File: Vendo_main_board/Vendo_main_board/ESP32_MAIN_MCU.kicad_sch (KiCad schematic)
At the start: 9 parts, among them SW1 SW_Push, SW2 SW_Push, U6 ESP32-WROOM-32

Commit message: -
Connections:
- no-connect marks 8 -> 10
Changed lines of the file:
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@@
+	)
+	(no_connect
+		(at 152.1704 95.8039)
+	)
+	(no_connect
+		(at 152.1704 78.0239)
 	)
 	(no_connect

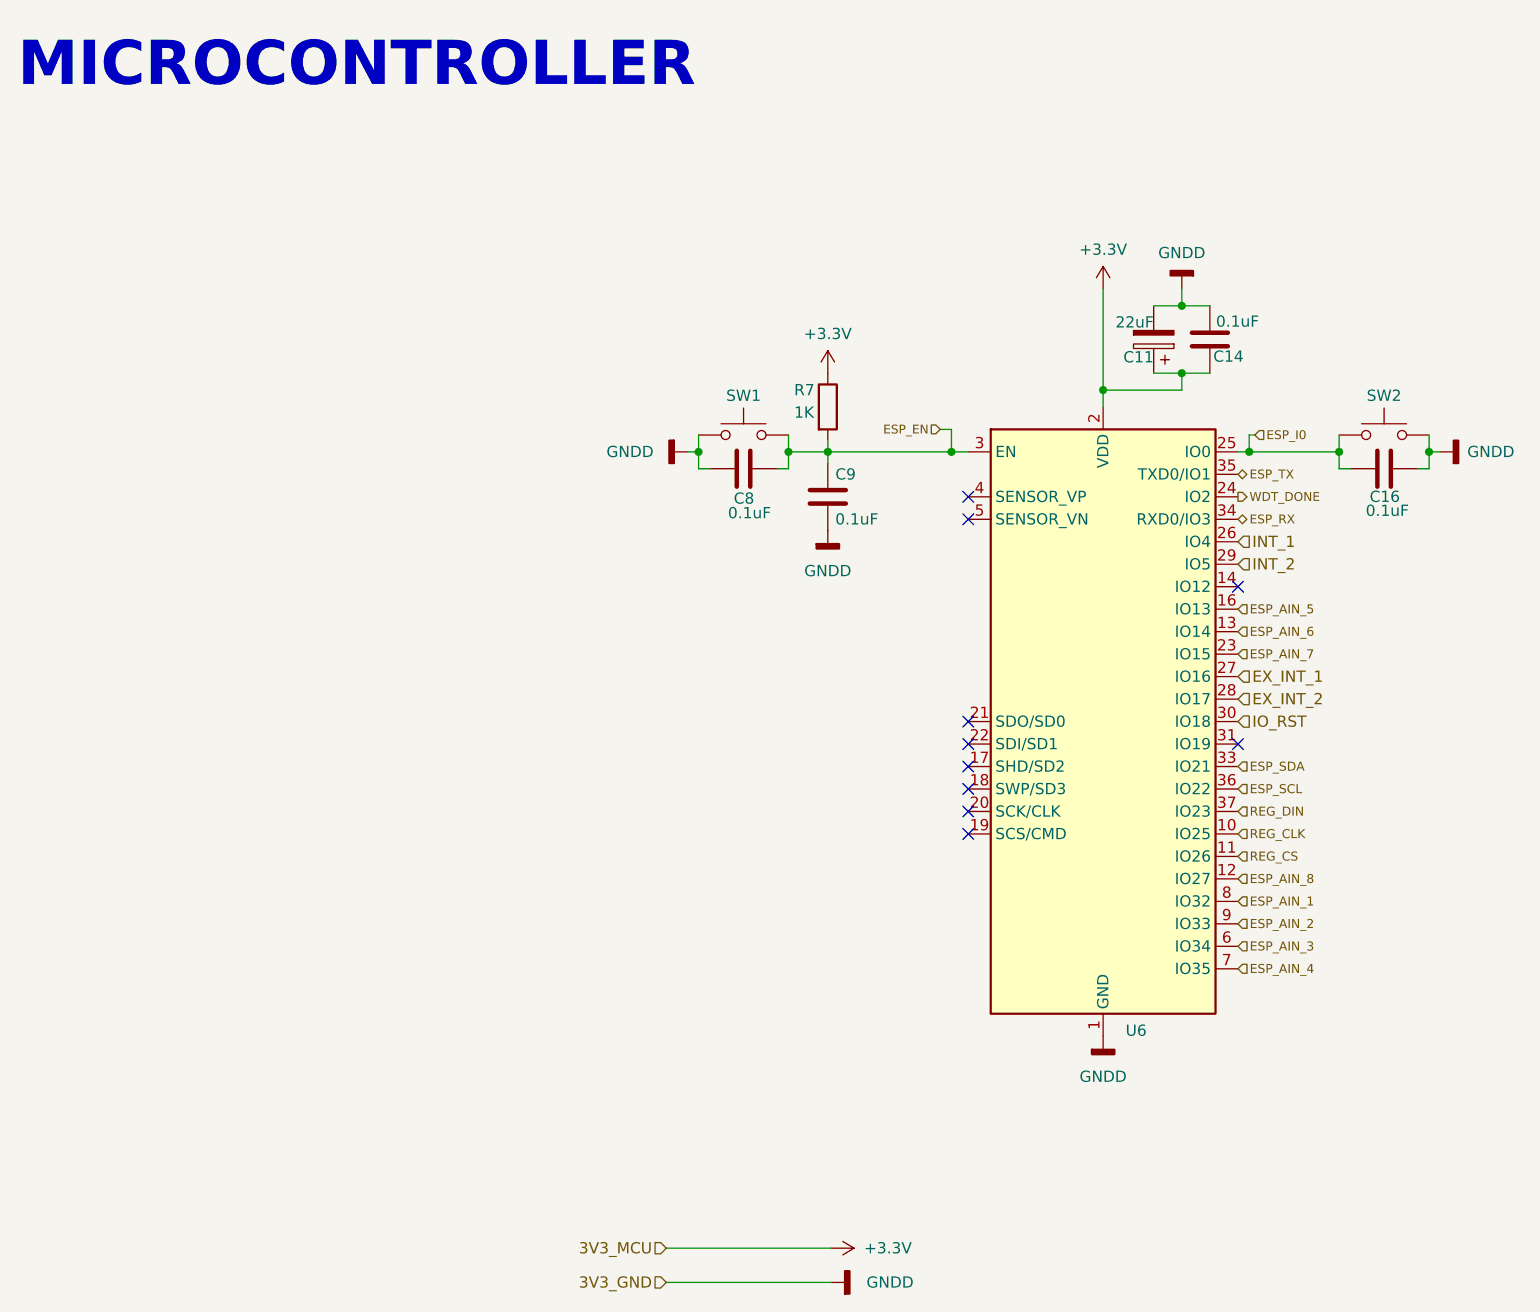
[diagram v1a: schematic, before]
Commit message: -update scheme and pcb placement
update scheme and footprint
added spade connectors
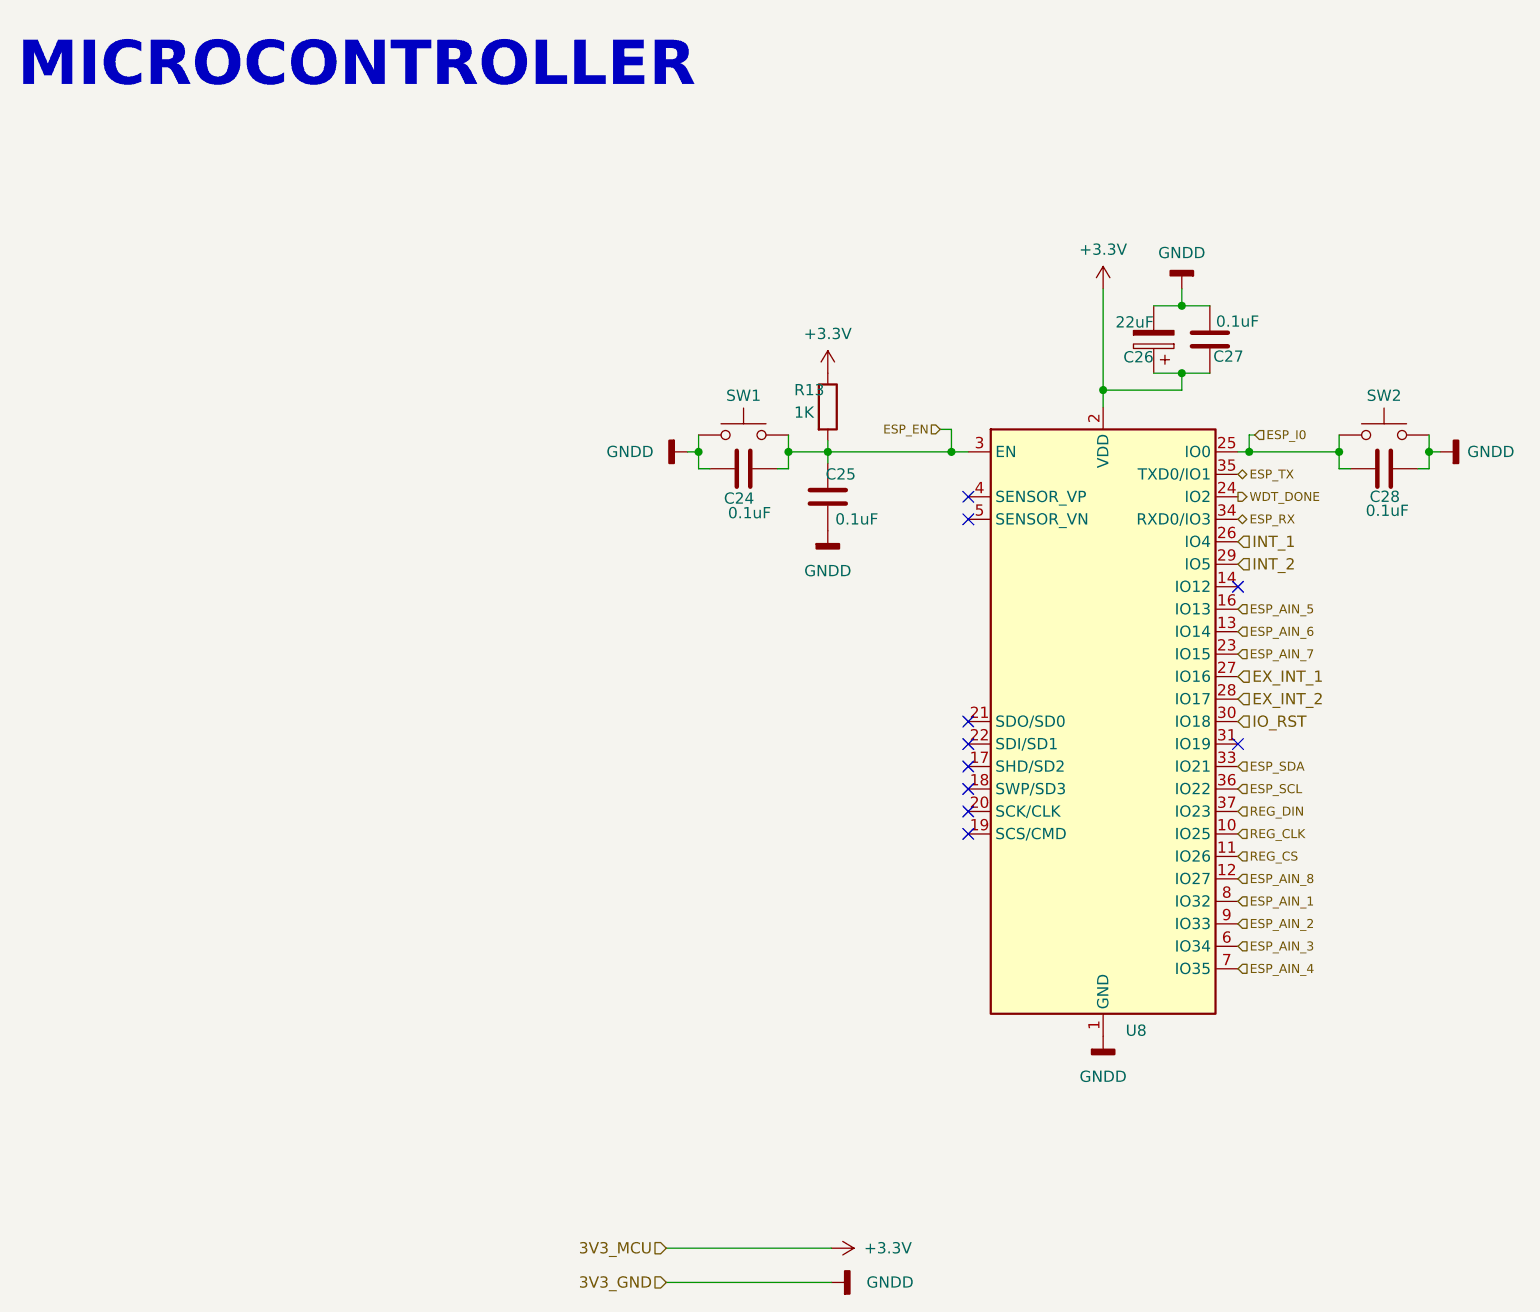
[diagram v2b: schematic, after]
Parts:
- renumbered C8 to C24, C9 to C25, C11 to C26, C14 to C27, C16 to C28, R7 to R13, U6 to U8
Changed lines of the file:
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@@
 		(on_board yes)
 		(dnp no)
-		(property "Reference" "#PWR018"
+		(property "Reference" "#PWR061"
 			(at 83.5904 62.7839 0)
 			(effects
@@
 			(project "Vendo_main_board"
 				(path "/ce68e045-3b24-4b1f-b4c3-20bce3f1de80/ce347859-48f7-466a-9120-8271178b4c4c"
-					(reference "#PWR018")
+					(reference "#PWR061")
 					(unit 1)
 				)
@@
 		(on_board yes)
 		(dnp no)
-		(property "Reference" "C14"
+		(property "Reference" "C27"
 			(at 152.809 52.0099 0)
 			(effects
@@
 			(project "Vendo_main_board"
 				(path "/ce68e045-3b24-4b1f-b4c3-20bce3f1de80/ce347859-48f7-466a-9120-8271178b4c4c"
-					(reference "C14")
+					(reference "C27")
 					(unit 1)
 				)
@@
 		(dnp no)
 		(fields_autoplaced yes)
-		(property "Reference" "#PWR024"
+		(property "Reference" "#PWR063"
 			(at 105.8154 78.0239 0)
 			(effects
@@
 			(project "Vendo_main_board"
 				(path "/ce68e045-3b24-4b1f-b4c3-20bce3f1de80/ce347859-48f7-466a-9120-8271178b4c4c"
-					(reference "#PWR024")
+					(reference "#PWR063")
 					(unit 1)
 				)
@@
 		(on_board yes)
 		(dnp no)
-		(property "Reference" "C16"
+		(property "Reference" "C28"
 			(at 170.4814 67.8532 90)
 			(effects
@@
 			(project "Vendo_main_board"
 				(path "/ce68e045-3b24-4b1f-b4c3-20bce3f1de80/ce347859-48f7-466a-9120-8271178b4c4c"
-					(reference "C16")
+					(reference "C28")
 					(unit 1)
 				)
@@
 		(dnp no)
 		(fields_autoplaced yes)
-		(property "Reference" "#PWR0119"
+		(property "Reference" "#PWR065"
 			(at 112.5847 156.6478 0)
 			(effects
@@
 			(project "Vendo_main_board"
 				(path "/ce68e045-3b24-4b1f-b4c3-20bce3f1de80/ce347859-48f7-466a-9120-8271178b4c4c"
-					(reference "#PWR0119")
+					(reference "#PWR065")
 					(unit 1)
 				)
@@
 		(on_board yes)
 		(dnp no)
-		(property "Reference" "C8"
+		(property "Reference" "C24"
 			(at 97.5063 68.053 90)
 			(effects
@@
 			(project "Vendo_main_board"
 				(path "/ce68e045-3b24-4b1f-b4c3-20bce3f1de80/ce347859-48f7-466a-9120-8271178b4c4c"
-					(reference "C8")
+					(reference "C24")
 					(unit 1)
 				)
@@
 		(dnp no)
 		(fields_autoplaced yes)
-		(property "Reference" "#PWR038"
+		(property "Reference" "#PWR069"
 			(at 181.3804 62.7839 0)
 			(effects
@@
 			(project "Vendo_main_board"
 				(path "/ce68e045-3b24-4b1f-b4c3-20bce3f1de80/ce347859-48f7-466a-9120-8271178b4c4c"
-					(reference "#PWR038")
+					(reference "#PWR069")
 					(unit 1)
 				)
@@
 		(dnp no)
 		(fields_autoplaced yes)
-		(property "Reference" "#PWR023"
+		(property "Reference" "#PWR062"
 			(at 105.8154 57.7039 0)
 			(effects
@@
 			(project "Vendo_main_board"
 				(path "/ce68e045-3b24-4b1f-b4c3-20bce3f1de80/ce347859-48f7-466a-9120-8271178b4c4c"
-					(reference "#PWR023")
+					(reference "#PWR062")
 					(unit 1)
 				)
@@
 		(on_board yes)
 		(dnp no)
-		(property "Reference" "C9"
+		(property "Reference" "C25"
 			(at 108.9904 65.3239 0)
 			(effects
@@
 			(project "Vendo_main_board"
 				(path "/ce68e045-3b24-4b1f-b4c3-20bce3f1de80/ce347859-48f7-466a-9120-8271178b4c4c"
-					(reference "C9")
+					(reference "C25")
 					(unit 1)
 				)
@@
 		(dnp no)
 		(fields_autoplaced yes)
-		(property "Reference" "#PWR029"
+		(property "Reference" "#PWR066"
 			(at 136.9304 48.1789 0)
 			(effects
@@
 			(project "Vendo_main_board"
 				(path "/ce68e045-3b24-4b1f-b4c3-20bce3f1de80/ce347859-48f7-466a-9120-8271178b4c4c"
-					(reference "#PWR029")
+					(reference "#PWR066")
 					(unit 1)
 				)
@@
 		(dnp no)
 		(fields_autoplaced yes)
-		(property "Reference" "#PWR0118"
+		(property "Reference" "#PWR064"
 			(at 102.4247 152.7784 0)
 			(effects
@@
 			(project "Vendo_main_board"
 				(path "/ce68e045-3b24-4b1f-b4c3-20bce3f1de80/ce347859-48f7-466a-9120-8271178b4c4c"
-					(reference "#PWR0118")
+					(reference "#PWR064")
 					(unit 1)
 				)
@@
 		(on_board yes)
 		(dnp no)
-		(property "Reference" "U6"
+		(property "Reference" "U8"
 			(at 139.4704 128.1889 0)
 			(effects
@@
 			(project "Vendo_main_board"
 				(path "/ce68e045-3b24-4b1f-b4c3-20bce3f1de80/ce347859-48f7-466a-9120-8271178b4c4c"
-					(reference "U6")
+					(reference "U8")
 					(unit 1)
 				)
@@
 		(on_board yes)
 		(dnp no)
-		(property "Reference" "C11"
+		(property "Reference" "C26"
 			(at 142.6454 52.0841 0)
 			(effects
@@
 			(project "Vendo_main_board"
 				(path "/ce68e045-3b24-4b1f-b4c3-20bce3f1de80/ce347859-48f7-466a-9120-8271178b4c4c"
-					(reference "C11")
+					(reference "C26")
 					(unit 1)
 				)
@@
 		(on_board yes)
 		(dnp no)
-		(property "Reference" "R7"
+		(property "Reference" "R13"
 			(at 102.0054 55.7989 0)
 			(effects
@@
 			(project "Vendo_main_board"
 				(path "/ce68e045-3b24-4b1f-b4c3-20bce3f1de80/ce347859-48f7-466a-9120-8271178b4c4c"
-					(reference "R7")
+					(reference "R13")
 					(unit 1)
 				)
@@
 		(dnp no)
 		(fields_autoplaced yes)
-		(property "Reference" "#PWR030"
+		(property "Reference" "#PWR067"
 			(at 136.9304 135.1739 0)
 			(effects
@@
 			(project "Vendo_main_board"
 				(path "/ce68e045-3b24-4b1f-b4c3-20bce3f1de80/ce347859-48f7-466a-9120-8271178b4c4c"
-					(reference "#PWR030")
+					(reference "#PWR067")
 					(unit 1)
 				)
@@
 		(dnp no)
 		(fields_autoplaced yes)
-		(property "Reference" "#PWR032"
+		(property "Reference" "#PWR068"
 			(at 145.8204 38.0189 0)
 			(effects
@@
 			(project "Vendo_main_board"
 				(path "/ce68e045-3b24-4b1f-b4c3-20bce3f1de80/ce347859-48f7-466a-9120-8271178b4c4c"
-					(reference "#PWR032")
-					(unit 1)
-				)
+					(reference "#PWR068")
+					(unit 1)
+				)
